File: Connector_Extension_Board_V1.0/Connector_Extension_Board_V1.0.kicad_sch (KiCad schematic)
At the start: 16 parts

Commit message: Hoan thanh SCH lan 1
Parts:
- removed BAT1: Conn_01x02, Library:CONN02_1723103302_MOL, symbol Connector_Generic:Conn_01x02
- removed Compute1: Conn_01x02, Library:TE_5-104809-1, symbol Connector_Generic:Conn_01x02
- removed JP1, JP2, JP3, JP4: Jumper_2_Bridged, Library:SolderJumper-2_P1.3mm_Bridged_RoundedPad1.0x1.5mm, symbol Jumper:Jumper_2_Bridged
- removed TP1, TP2, TP3: ~, Library:TestPoint_Pad_D1.0mm, symbol Connector:TestPoint
- removed Winch2, Winch3, Winch4, Winch5: Conn_01x02, Library:MOLEX_1722871102, symbol Connector_Generic:Conn_01x02
- added C1, C12, C13, C14, C15, C16, C17, C18, C19, C2, C23, C24, C25, C3, C4, C5: 10u/50V/1206, symbol Device:C
- added C10: 5.6n/50V/0603, Library:C_0603_1608Metric, symbol Device:C
- added C11: 1n/50V/0603, Library:C_0603_1608Metric, symbol Device:C
- added C20, C21, C22, C6, C7, C8, C9: 47n/50V/0603, symbol Device:C
- added Computer1, Lidar1, Square1: WM11839-ND, Library:MOLEX_1722871102, symbol Connector_Generic:Conn_01x02
- added J1: 02519031301, symbol Connector_Generic:Conn_01x03
- added R1, R10, R11, R12, R13, R17, R18, R19, R20, R21, R22, R6, R7, R8, R9: 10k/0603/1%, Library:R_0603_1608Metric, symbol Device:R
- added R14, R15, R4: 1.82k/0603/1%, Library:R_0603_1608Metric, symbol Device:R
- added R16: 2.8k/0603/1%, Library:R_0603_1608Metric, symbol Device:R
- added R2: 8.25k/0603/1%, Library:R_0603_1608Metric, symbol Device:R
- added R3: 4.53k/0603/1%, Library:R_0603_1608Metric, symbol Device:R
- added R5: 2.21k/0603/1%, Library:R_0603_1608Metric, symbol Device:R
- added TP1, TP2: Lora, symbol Connector:TestPoint_Alt
- added TP3, TP4: Spare, symbol Connector:TestPoint_Alt
- added U1, U2, U3, U4, U6, U7, U8: SIP32433ADN-T1E4, DFN-10_3X3_VIS, symbol Library:SIP32433ADN-T1E4
- added U5: AOZ13984DI-02, symbol Library:AOZ13984DI-02
- Winch1: value Conn_01x02 -> WM11839-ND
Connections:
- net GND: now also C1.2, C10.2, C11.2, C12.2, C13.2, C14.2, C15.2, C16.2, C17.2, C18.2, C19.2, C2.2, C20.2, C21.2, C22.2, C23.2, C24.2, C25.2, C3.2, C4.2, C5.2, C6.2, C7.2, C8.2, C9.2, Computer1.2 (Pin_2), J1.3 (Pin_3), Lidar1.2 (Pin_2), R14.1, R15.1, R16.1, R2.1, R3.1, R4.1, R5.1, Square1.2 (Pin_2), TP2.1, TP4.1, U1.11 (PAD), U1.6 (GND), U2.11 (PAD), U2.6 (GND), U3.11 (PAD), U3.6 (GND), U4.11 (PAD), U4.6 (GND), U5.13 (EXP), U5.6 (GND), U6.11 (PAD), U6.6 (GND), U7.11 (PAD), U7.6 (GND), U8.11 (PAD), U8.6 (GND)
- net 5V_REG_2/V_OUT renamed +5V-2A
- net +5V-2A: now also C25.1, U8.10 (Vout), U8.9 (Vout)
- net 5V_REG_3/V_OUT renamed +5V-3A_1
- net +5V-3A_1: now also C24.1, U7.10 (Vout), U7.9 (Vout)
- net WINCH_REG/VOUT renamed +12V-5A
- net +12V-5A: now also C13.1, U5.1 (Vout), U5.2 (Vout)
- new net: C20.1, U6.3 (SS)
- new net: R14.2, U6.5 (ILim)
- new net: R18.1, U6.7 (~{PG})
- new net: R17.1, U6.8 (~{FLG})
- new net: C9.1, U4.3 (SS)
- new net: R5.2, U4.5 (ILim)
- new net: R13.1, U4.7 (~{PG})
- new net: R12.1, U4.8 (~{FLG})
- new net: R2.2, U1.5 (ILim)
- new net: R19.1, U7.8 (~{FLG})
- new net: R11.1, U3.7 (~{PG})
- new net: R3.2, U2.5 (ILim)
- new net: R21.1, U8.8 (~{FLG})
- new net: R22.1, U8.7 (~{PG})
- new net: C7.1, U2.3 (SS)
- new net: R9.1, U2.7 (~{PG})
- new net: R8.1, U2.8 (~{FLG})
- new net: C8.1, U3.3 (SS)
- new net: R4.2, U3.5 (ILim)
- new net: R10.1, U3.8 (~{FLG})
- new net: C10.1, U5.7 (SS)
- new net: R16.2, U8.5 (ILim)
- new net: C22.1, U8.3 (SS)
- new net: R1.2, U5.8 (FLTB )
- new net: C11.1, U5.4 (CAP)
- new net: R20.1, U7.7 (~{PG})
- new net: R7.1, U1.7 (~{PG})
- new net: C21.1, U7.3 (SS)
- new net: R15.2, U7.5 (ILim)
- new net: R6.1, U1.8 (~{FLG})
- new net: C6.1, U1.3 (SS)
- new net +12V: C1.1, C2.1, C3.1, C4.1, C5.1, J1.2 (Pin_2), U1.1 (Vin), U1.2 (Vin), U2.1 (Vin), U2.2 (Vin), U3.1 (Vin), U3.2 (Vin), U4.1 (Vin), U4.2 (Vin), U5.10 (Vin), U5.9 (Vin)
- new net +12V-0.2A: C12.1, TP1.1, U1.10 (Vout), U1.9 (Vout)
- new net +12V-1A: C14.1, Square1.1 (Pin_1), U2.10 (Vout), U2.9 (Vout)
- new net +12V-2.5A: C16.1, Lidar1.1 (Pin_1), U4.10 (Vout), U4.9 (Vout)
- new net +12V-3A: C15.1, Computer1.1 (Pin_1), U3.10 (Vout), U3.9 (Vout)
- new net +5V: C17.1, C18.1, C19.1, J1.1 (Pin_1), R1.1, R10.2, R11.2, R12.2, R13.2, R17.2, R18.2, R19.2, R20.2, R21.2, R22.2, R6.2, R7.2, R8.2, R9.2, U1.4 (EN), U2.4 (EN), U3.4 (EN), U4.4 (EN), U5.5 (EN), U6.1 (Vin), U6.2 (Vin), U6.4 (EN), U7.1 (Vin), U7.2 (Vin), U7.4 (EN), U8.1 (Vin), U8.2 (Vin), U8.4 (EN)
- new net +5V-3A_2: C23.1, TP3.1, U6.10 (Vout), U6.9 (Vout)
- no-connect marks 8 -> 10
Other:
- removed sheet 5V_REG_1
- removed sheet 5V_REG_2
- removed sheet 5V_REG_3
- removed sheet LIDAR_REG
- removed sheet WINCH_REG
- note added: "0.75A"
- note added: "1.37"
- note added: "12V-0.2A"
- note added: "12V-1A"
- note added: "12V-2.5A"
- note added: "12V-3A"
- note added: "12V-5A"
- note added: "2.21A"
- note added: "2.81A"
- note added: "3.41A"
- note added: "5V-2A"
- note added: "5V-3A"
- note added: "VIN"
- note removed: "12V 180W Max"
- note removed: "12V 30W Peak"
- note removed: "16V Minimum Voltage 250W Peak draw 15.6A peak"
- note removed: "5V 15W Peak"
- note removed: "GPS Module 3A Peak 0.5A Nom."
- note removed: "LIVOX Lidar 2.5A Peak 0.9A Nom."
- note removed: "Latte Panda 3A Peak 2A Nom."
- note removed: "Mating Housing Molex Ultra-Fit 1722563102 DK:WM26332-ND N.B Polarity difference to 12V con."
- note removed: "Milwaukee 18V 5S LiPo pack 21V-16V"
- note removed: "Peltier 3A Nom."
- note removed: "Reel Motor 9.72A Peak 2.5A Nom. SiC437"

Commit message: Chỉnh sủa SCH 24/12
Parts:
- removed C1, C2, C23, C24, C25, C3: 10u/50V/1206, symbol Device:C
- removed R1, R18, R20, R21, R22: 10k/0603/1%, Library:R_0603_1608Metric, symbol Device:R
- removed R14, R15: 1.82k/0603/1%, Library:R_0603_1608Metric, symbol Device:R
- removed R2: 8.25k/0603/1%, Library:R_0603_1608Metric, symbol Device:R
- removed R3: 4.53k/0603/1%, Library:R_0603_1608Metric, symbol Device:R
- removed U1, U2, U6, U7: SIP32433ADN-T1E4, DFN-10_3X3_VIS, symbol Library:SIP32433ADN-T1E4
- removed U5: AOZ13984DI-02, symbol Library:AOZ13984DI-02
- added C26: 100nF/50V/0603, symbol Device:C
- added C27, C28: 10u/50V/1206, symbol Device:C
- added R23: 12.7k/0603/1%, Library:R_0603_1608Metric, symbol Device:R
- added R24: 10k/0603/1%, Library:R_0603_1608Metric, symbol Device:R
- added R25, R37: 1k/0603/1%, Library:R_0603_1608Metric, symbol Device:R
- added R26, R27, R28: 4.99k/0603/1%, Library:R_0603_1608Metric, symbol Device:R
- added R29, R31, R33, R35, R38, R40, R42: 100k/0603/1%, Library:R_0603_1608Metric, symbol Device:R
- added R30, R32, R34, R36: 10.7k/0603/1%, Library:R_0603_1608Metric, symbol Device:R
- added R39, R41, R43: 4.87k/0603/1%, Library:R_0603_1608Metric, symbol Device:R
- added U10, U11, U12, U5: SIP32433ADN-T1E4, DFN-10_3X3_VIS, symbol Library:SIP32433ADN-T1E4
- added U9: TPS1HC30BQPWPRQ1, symbol Library:TPS1HC30BQPWPRQ1
- C10: value 5.6n/50V/0603 -> 120n/50V/0603; footprint Library:C_0603_1608Metric -> (none)
- C11: value 1n/50V/0603 -> 120n/50V/0603; footprint Library:C_0603_1608Metric -> (none)
- C13, C18: value 10u/50V/1206 -> 120n/50V/0603
- C20, C8, C9: value 47n/50V/0603 -> 120n/50V/0603
- C21, C22, C6, C7: value 47n/50V/0603 -> 10u/50V/1206
- J1: value 02519031301 -> 640388-3
- R10, R9: value 10k/0603/1% -> 1.8k/0603/1%
- R11, R12, R13, R17, R19: value 10k/0603/1% -> 1k/0603/1%
- R16: value 2.8k/0603/1% -> 1k/0603/1%
- R4: value 1.82k/0603/1% -> 1.8k/0603/1%
- R5: value 2.21k/0603/1% -> 2.05k/0603/1%
- R6: value 10k/0603/1% -> 6.19k/0603/1%
- R7: value 10k/0603/1% -> 2.43k/0603/1%
- R8: value 10k/0603/1% -> 4.12k/0603/1%
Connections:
- net +12V: now also C6.1, C7.1, C26.1, R29.1, R30.2, R31.1, R32.2, R33.1, R34.2, R35.1, R36.2, U10.1 (Vin), U10.2 (Vin), U5.1 (Vin), U5.2 (Vin), U9.12 (VBB), U9.13 (VBB__1)
- net +12V-0.2A: now also C28.1, U10.10 (Vout), U10.9 (Vout); no longer C12.1
- net +12V-1A: now also C27.1, U5.10 (Vout), U5.9 (Vout); no longer C14.1
- net +12V-2.5A: no longer Lidar1.1 (Pin_1)
- net +5V: now also C12.1, C14.1, R24.2, R26.1, R27.1, R28.1, R38.1, R39.2, R40.1, R41.2, R42.1, R43.2, U11.1 (Vin), U11.2 (Vin), U12.1 (Vin), U12.2 (Vin); no longer C18.1, C19.1, R10.2, R11.2, R12.2, R13.2, R17.2, R19.2, R6.2, R7.2, R8.2, R9.2, U3.4 (EN), U4.4 (EN), U8.4 (EN)
- net +5V-2A: now also C19.1
- net +5V-3A_1: now also C21.1, U11.10 (Vout), U11.9 (Vout)
- net +5V-3A_2: now also C22.1, U12.10 (Vout), U12.9 (Vout)
- net GND: now also R10.1, R11.1, R12.1, R13.1, R17.1, R19.1, R6.1, R7.1, R8.1, R9.1, C26.2, C27.2, C28.2, R23.1, R25.2, R37.1, U10.11 (PAD), U10.6 (GND), U11.11 (PAD), U11.6 (GND), U12.11 (PAD), U12.6 (GND), U5.11 (PAD), U5.6 (GND), U9.1 (GND), U9.15 (EXP)
- net at C20.1: now also U12.3 (SS)
- net at U4.7 (OVP): now also R12.2, R32.1; no longer R13.1
- net at U4.8 (PG): no longer R12.1
- net at U3.7 (OVP): now also R11.2, R30.1; no longer R11.1
- net at U8.7 (OVP): now also R16.2, R39.1
- net at U3.8 (PG): no longer R10.1
- net at C10.1: now also U5.3 (SS)
- net at U8.5 (ILim): now also R7.2; no longer R16.2
- net at U8.3 (SS): now also C13.1; no longer C22.1
- net at C11.1: now also U10.3 (SS)
- net +12V-5A renamed +12V-7A
- net +12V-7A: now also U9.10 (VOUT__1), U9.9 (VOUT); no longer C13.1
- new net: R9.2, U11.5 (ILim)
- new net: R28.2, U9.2 (EN)
- new net: R33.2, U5.4 (EN/UVLO)
- new net: R13.2, R34.1, U5.7 (OVP)
- new net: R40.2, U11.4 (EN/UVLO)
- new net: R17.2, R43.1, U12.7 (OVP)
- new net: R26.2, U9.5 (LATCH)
- new net: R8.2, U5.5 (ILim)
- new net: R19.2, R41.1, U11.7 (OVP)
- new net: R35.2, U10.4 (EN/UVLO)
- new net: R6.2, U10.5 (ILim)
- new net: R36.1, R37.2, U10.7 (OVP)
- new net: R10.2, U12.5 (ILim)
- new net: R38.2, U8.4 (EN/UVLO)
- new net: R29.2, U3.4 (EN/UVLO)
- new net: R42.2, U12.4 (EN/UVLO)
- new net: R27.2, U9.3 (DIAG_EN)
- new net: R31.2, U4.4 (EN/UVLO)
- new net: C18.1, U11.3 (SS)
- new net: R24.1, U9.4 (~{FAULT})
- new net: R25.1, U9.6 (SNS)
- new net: R23.2, U9.7 (ILIM)
- no-connect marks 10 -> 15
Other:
- note added: "12V-7A"
- note added: "BACKup: 350790-1"
- note added: "ILim=(0.6/RLim)*10300 0.99A"
- note added: "ILim=(0.6/RLim)*10300 1.5A"
- note added: "ILim=(0.6/RLim)*10300 2.54A"
- note added: "ILim=(0.6/RLim)*10300 3.01A"
- note added: "ILim=(0.6/RLim)*10300 3.43A"
- note added: "Ilim=90/RLim 90/12.7=7.08A"
- note added: "Imax: 14.4A Pitch: 3.96mm"
- note added: "OVP: 14.04V"
- note added: "OVP: 7.04V"
- note added: "Since a 1% resistor is used, the E92 standard values are applied."
- note removed: "0.75A"
- note removed: "1.37"
- note removed: "12V-5A"
- note removed: "2.21A"
- note removed: "2.81A"
- note removed: "3.41A"
- company: Raw Matter IO Pty Ltd -> (none)
- title: Diptek 5S LiPo Power distribution  -> Diptek Connector Extension Board
- moved on the sheet: R11, Winch1

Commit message: Hoan thanh footprint
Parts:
- C10, C11, C13, C18, C20, C26, C8, C9: footprint (none) -> Capacitor_SMD:C_0603_1608Metric
- C12, C14, C15, C16, C17, C19, C21, C22, C27, C28, C4, C5, C6, C7: footprint (none) -> Capacitor_SMD:C_1206_3216Metric
- Computer1, Lidar1, Winch1: value WM11839-ND -> 1723103102; footprint Library:MOLEX_1722871102 -> Library:MOLEX_1723103102; DIGIKEY (none) -> 900-1723103102-ND; Digikey WM11839-ND -> 900-1723103102-ND
- GPS1, Phone1: footprint Library:TE_5-104809-1 -> Library:TE_5-104361-1; DIGIKEY (none) -> A33961-ND
- J1: footprint (none) -> Library:TE_640388-3
- R10, R11, R12, R13, R16, R17, R19, R23, R24, R25, R26, R27, R28, R29, R30, R31, R32, R33, R34, R35, R36, R37, R38, R39, R4, R40, R41, R42, R43, R5, R6, R7, R8, R9: footprint Library:R_0603_1608Metric -> Resistor_SMD:R_0603_1608Metric
- Spare1: renamed from Square1; value WM11839-ND -> 1723103102; footprint Library:MOLEX_1722871102 -> Library:MOLEX_1723103102; DIGIKEY (none) -> 900-1723103102-ND; Digikey WM11839-ND -> 900-1723103102-ND
- TP1, TP2: footprint (none) -> Library:TestPoint_Loop_D2.50mm_Drill1.0mm; now not fitted; now left out of the parts list
- TP3, TP4: footprint (none) -> Library:TestPoint_Loop_D2.50mm_Drill1.0mm; now not fitted
- U10, U11, U12, U3, U4, U5, U8: footprint DFN-10_3X3_VIS -> Library:DFN-10-1EP_3x3mm_P0.5mm_EP1.7x2.5mm
- U9: footprint (none) -> Library:IC_TPS1HC30BQPWPRQ1; DIGIKEY (none) -> 296-TPS1HC30BQPWPRQ1CT-ND
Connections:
- net +12V-2.5A: now also Lidar1.1 (Pin_1)
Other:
- moved on the sheet: Lidar1

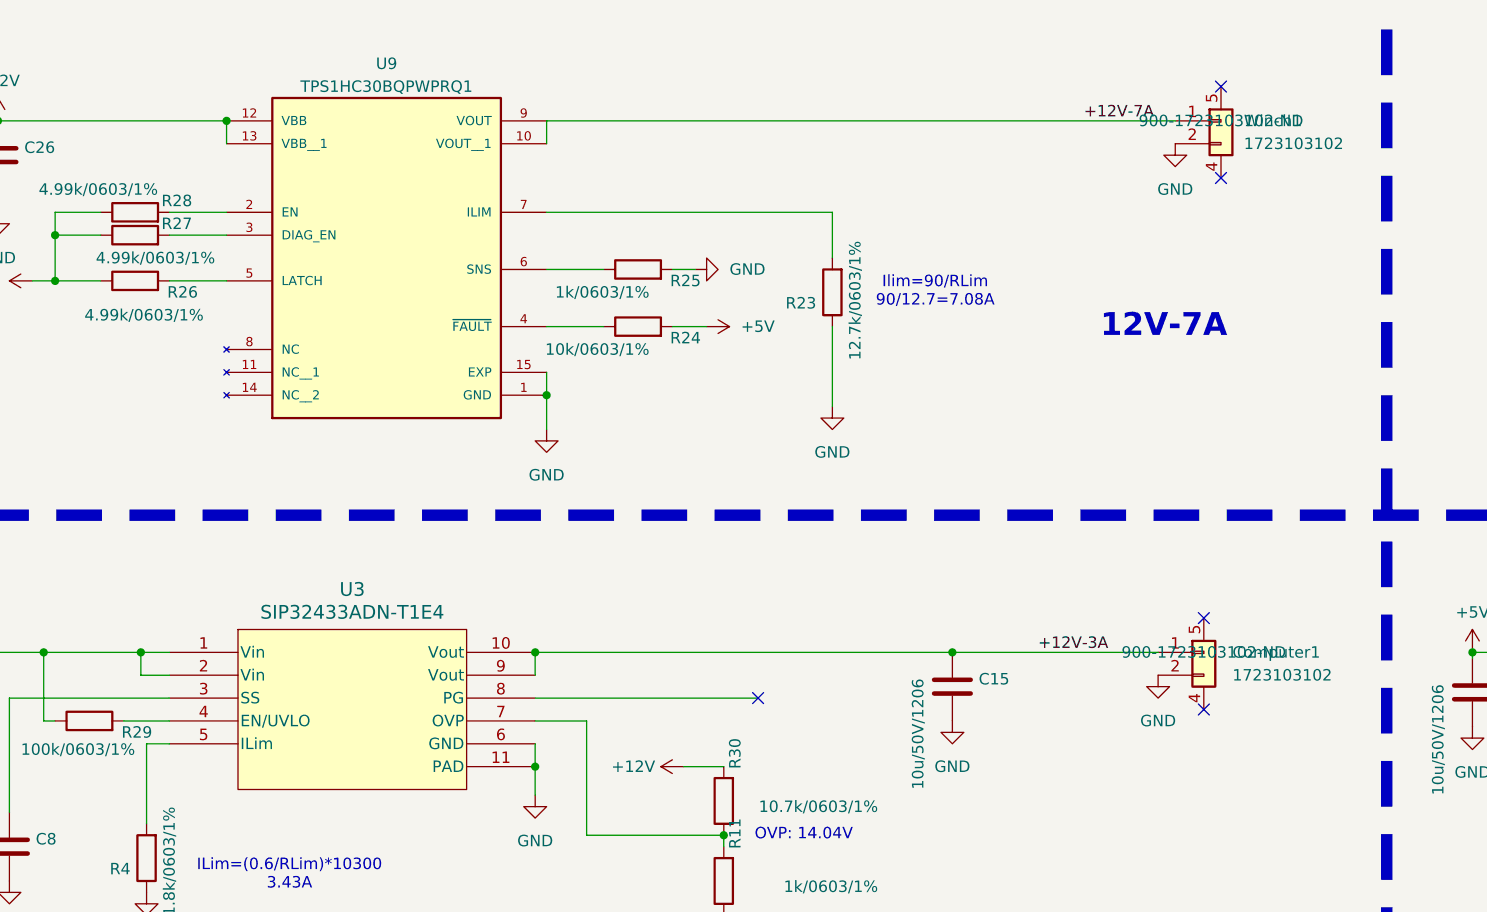
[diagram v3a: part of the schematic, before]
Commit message: Cập nhật connecter 12 5
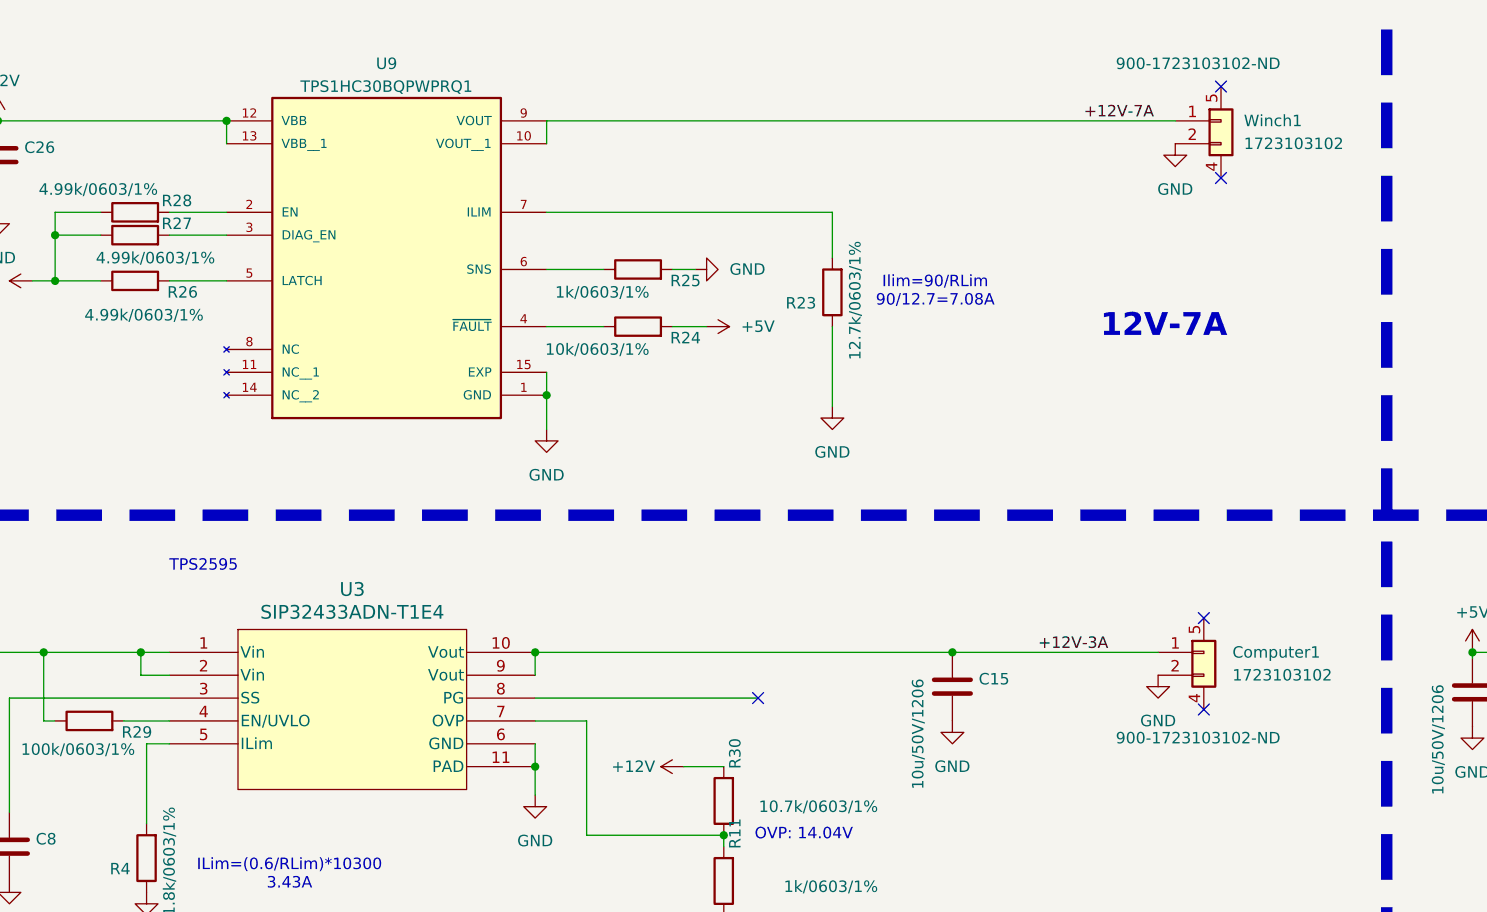
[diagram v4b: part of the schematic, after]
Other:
- note added: "TPS2595"
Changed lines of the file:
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@@
 		)
 	)
+	(text "TPS2595"
+		(exclude_from_sim no)
+		(at 110.49 72.39 0)
+		(effects
+			(font
+				(size 1.27 1.27)
+			)
+		)
+	)
 	(text "ILim=(0.6/RLim)*10300\n3.01A"
 		(exclude_from_sim no)
@@
 			"MQBlAGUAKwA5ADEANQA0AEkAcgBoAG8ALwBSADQASABMAEUAZABUAEcAZAB0AG0AKwA5ADkAVgBi"
 			"AHgAbABRAE4AWQBMAHAAYwBYAEYAeABkADkAMwA1AGMAegBYADgASQB4AFUAMABvAGgAaABNADEA"
-			"bQBVAHcAcABtAGoAawBhAHIAZgBVAHYAVABlAFAANgBMAFkALwAxAHAAdQ=="
+			"bQBVAHcAcABtAGoAawBhAHIAZgBVAHYAVABlAFAANgBMAFkALwAxAHAAdQBkAC8ANQBzAG8AZQBV"
+			"AFUAcABrADIANwBHADkANQB4AEYAZQBKADUAOQBFADgAMgBrAHAAWQA3AFEAaABLAEMAYgBVAGUA"
+			"SgB4AE4AagB6AFAAWABXAEoASgBtADMASQBSAFQAagBiAEwASgA4AE4AOABiAEkASQBpAHkAUwA5"
+			"AHcAcQBVAGgAMgBFAG8AbgAxADUAYwBYAEMAdwBXAGkALwBHAHAAbgBrAHcAbQBYAC8AYgBqADcA"
+			"UgB5AGIAVwBRAGkAaABwAEwAKwBOAGgAMQBsAFYAVgBjADYANQBzAE0ALwBkAGwAcQA2AHUANgAw"
+			"AEoATQBYADMAMgBVAHAAOQBvADUANQA3ADAAdgAwAFMAMABwAHAAUwBLAGIAWAB6AGEANAA5AEcA"
+			"UwBPAEUAOABIAEMATQBvAG0AbwArAEQATABtADgAMwBtAFoAegBZAC8AUgBFAFcAVQBxAEcAVgBQ"
+			"AGcAWABTAEkANQBFAFIASwAyAC8ARgBDAGgAWQBuAEEARQBJAHgASgBGAFMAVABUAFAAWgB1AEkA"
+			"cgBFAEIATwBwAEUARABLAGoAMQBHAFIAWABoAHUAbQAyAHoAcwBUAFcAZQA3ADUAbABxAEcAcQBr"
+			"ACsAbABUAGgAawBDAE8ATwBPAE8ASwBJAEkANwA0AHkAbgBKACsAZgBwADQAVABOAFoAbABPAEcA"
+			"KwA1AFQAUwBsAHMARABKADEAZABrADIATgAyAC8AZQBIAEcATQBvAEMAegBFAHQAUQBaAG4ARgBO"
+			"AGgAeABDAEcASgBVADEAbQA2AGEAcABxAHUAcgBoAHcANABkAGwAawBHAHEAYQBSAGsAVAA2AHYA"
+			"bwA4AHgATABwAGYATABrAG0AYQBPAEoAeABNAHoAOQBwAG4AaQBwAFMAdwBSAEgATwBDAGEAWgBi"
+			"AHkANwBsAEUAegB5AGMAegB4AG4AZQBBAFgAeABQAEoAcABIAEkAMQBrAHMAWgB2AEIAeQA4ADIA"
+			"RgBuADIAUwA1AEIAMAA2AFYANgArAEQAagA1AEsATABmAG0AVwBCADgASQB3AEcAYQB6AFcAYQA5"
+			"AFcAMAA5AGwAcwBHAEkAWgBxAEYAMwA1AFIAYgBOADEATgBVAHgAWAB6AFoAOQBGAFUASwBrADYA"
+			"TgBmAGMAMgBqAEwAdwBNAHAANgBjAGMAZgBmADMAcgB2ADMAcgAxAHgASQBrAHQARQBLAGUAWAB4"
+			"AGIAbQBSAEcAWABkAGQAZABOAHgAQwBoAEIAUABGADgAcQBmADEANQBVAFIAaQBHAG8AZQB2AGkA"
+			"ZQByADAAdQBqAC8AVAA0AGQASgBYAEwAZABNAG0AWQBDAHEARAB2ACsANg=="
 		)
 	)
@@
 		(on_board yes)
 		(dnp no)
-		(fields_autoplaced yes)
 		(property "Reference" "Winch1"
 			(at 226.06 22.8599 0)
@@
 		)
 		(property "DIGIKEY" "900-1723103102-ND"
-			(at 223.52 22.86 0)
+			(at 220.98 16.51 0)
 			(effects
 				(font
@@
 		(on_board yes)
 		(dnp no)
-		(fields_autoplaced yes)
 		(property "Reference" "Computer1"
 			(at 224.79 81.9149 0)
@@
 		)
 		(property "DIGIKEY" "900-1723103102-ND"
-			(at 221.615 81.915 0)
+			(at 220.98 91.44 0)
 			(effects
 				(font
